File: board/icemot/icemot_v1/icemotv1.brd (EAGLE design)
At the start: 160 x 100 mm, 2 parts, among them U1 ICE40HX4K, U2 EFM32WG332FXXX-QFP64

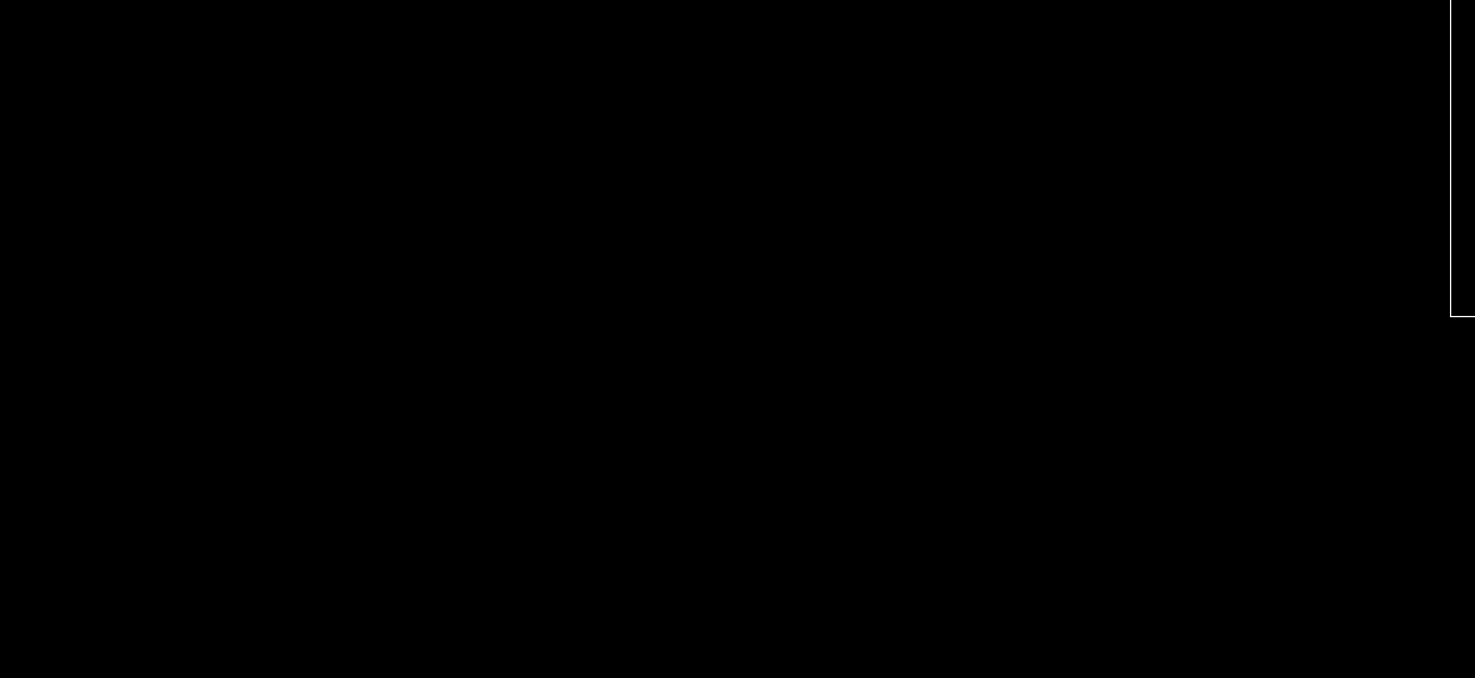
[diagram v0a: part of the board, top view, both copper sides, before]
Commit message: adding decoupling and usb connector
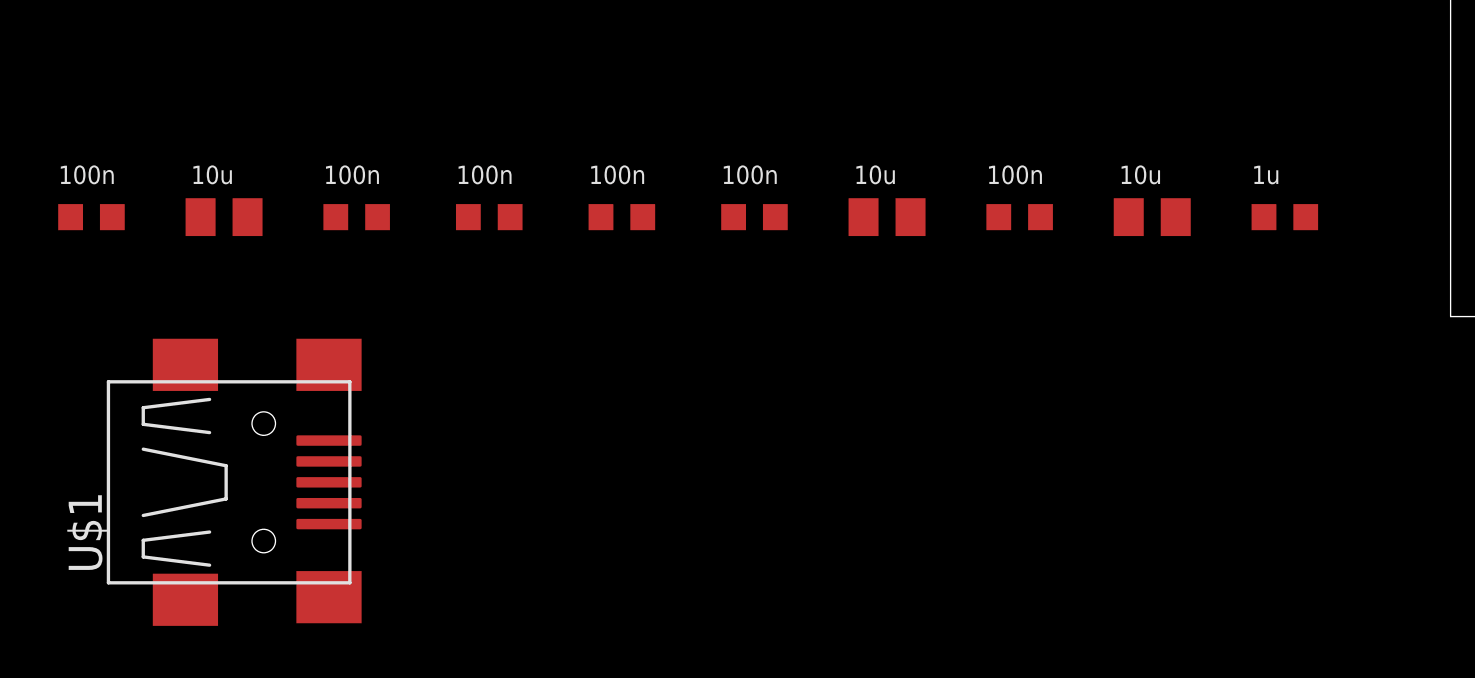
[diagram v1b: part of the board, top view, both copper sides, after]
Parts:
- added C1: 1u, standard_passive:R0603
- added C10, C3, C5, C6, C7, C8: 100n, standard_passive:R0603
- added C2, C4, C9: 10u, standard_passive:R0805
- added U$1: USB-SHIELD, usb-header:USB-M-S1
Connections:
- removed net DECOUPLE: U2.40
- removed net USBVREGI: U2.45
- removed net VDDREG: U2.39
- new net N$1: C1.1, U2.40
- new net N$2: U$1.D+, U2.48
- new net N$3: U$1.D-, U2.47
- new net N$4: U$1.VBUS, U2.45
- net +3V3: now also C10.2, C2.1, C3.1, C4.1, C5.1, C6.1, C7.1, C8.1, C9.1, U2.39
- net GND: now also C1.2, C10.1, C2.2, C3.2, C4.2, C5.2, C6.2, C7.2, C8.2, C9.2
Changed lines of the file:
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@@
 <element name="U1" library="ICE40HX" package="TQFP144" value="ICE40HX4K" x="45.72" y="48.26"/>
 <element name="U2" library="EFM32" package="TQFP64-0.5-12X12MM" value="EFM32WG332FXXX-QFP64" x="44.45" y="24.13"/>
+<element name="C1" library="standard_passive" package="R0603" value="1u" x="-6.35" y="3.81"/>
+<element name="C2" library="standard_passive" package="R0805" value="10u" x="-11.43" y="3.81"/>
+<element name="C3" library="standard_passive" package="R0603" value="100n" x="-16.51" y="3.81"/>
+<element name="C4" library="standard_passive" package="R0805" value="10u" x="-21.59" y="3.81"/>
+<element name="C5" library="standard_passive" package="R0603" value="100n" x="-26.67" y="3.81"/>
+<element name="C6" library="standard_passive" package="R0603" value="100n" x="-31.75" y="3.81"/>
+<element name="C7" library="standard_passive" package="R0603" value="100n" x="-36.83" y="3.81"/>
+<element name="C8" library="standard_passive" package="R0603" value="100n" x="-41.91" y="3.81"/>
+<element name="C9" library="standard_passive" package="R0805" value="10u" x="-46.99" y="3.81"/>
+<element name="C10" library="standard_passive" package="R0603" value="100n" x="-52.07" y="3.81"/>
+<element name="U$1" library="usb-header" package="USB-M-S1" value="USB-SHIELD" x="-45.72" y="-6.35"/>
 </elements>
 <signals>
@@
 <contactref element="U2" pad="56"/>
 <contactref element="U2" pad="8"/>
+<contactref element="C1" pad="2"/>
+<contactref element="C2" pad="2"/>
+<contactref element="C3" pad="2"/>
+<contactref element="C4" pad="2"/>
+<contactref element="C5" pad="2"/>
+<contactref element="C6" pad="2"/>
+<contactref element="C7" pad="2"/>
+<contactref element="C8" pad="2"/>
+<contactref element="C10" pad="1"/>
+<contactref element="C9" pad="2"/>
 <wire x1="56.32" y1="50.51" x2="56.32" y2="55.51" width="0" layer="19" extent="1-1"/>
 <wire x1="47.97" y1="58.86" x2="56.32" y2="55.51" width="0" layer="19" extent="1-1"/>
@@
 <wire x1="38.55" y1="24.38" x2="44.7" y2="30.03" width="0" layer="19" extent="1-1"/>
 <wire x1="43.2" y1="18.23" x2="38.55" y2="24.38" width="0" layer="19" extent="1-1"/>
+<wire x1="-5.55" y1="3.81" x2="38.55" y2="24.38" width="0" layer="19" extent="1-1"/>
+<wire x1="-10.53" y1="3.81" x2="-5.55" y2="3.81" width="0" layer="19" extent="1-1"/>
+<wire x1="-15.71" y1="3.81" x2="-10.53" y2="3.81" width="0" layer="19" extent="1-1"/>
+<wire x1="-20.69" y1="3.81" x2="-15.71" y2="3.81" width="0" layer="19" extent="1-1"/>
+<wire x1="-25.87" y1="3.81" x2="-20.69" y2="3.81" width="0" layer="19" extent="1-1"/>
+<wire x1="-30.95" y1="3.81" x2="-25.87" y2="3.81" width="0" layer="19" extent="1-1"/>
+<wire x1="-36.03" y1="3.81" x2="-30.95" y2="3.81" width="0" layer="19" extent="1-1"/>
+<wire x1="-41.11" y1="3.81" x2="-36.03" y2="3.81" width="0" layer="19" extent="1-1"/>
+<wire x1="-46.09" y1="3.81" x2="-41.11" y2="3.81" width="0" layer="19" extent="1-1"/>
+<wire x1="-52.87" y1="3.81" x2="-46.09" y2="3.81" width="0" layer="19" extent="1-1"/>
 </signal>
 <signal name="PLLGND">
@@
 <contactref element="U1" pad="109"/>
 </signal>
-<signal name="VDDREG">
-<contactref element="U2" pad="39"/>
-</signal>
-<signal name="DECOUPLE">
-<contactref element="U2" pad="40"/>
-</signal>
-<signal name="USBVREGI">
-<contactref element="U2" pad="45"/>
-</signal>
 <signal name="USBVREGO">
 <contactref element="U2" pad="46"/>
@@
 <contactref element="U2" pad="26"/>
 <contactref element="U2" pad="27"/>
+<contactref element="U2" pad="39"/>
+<contactref element="C3" pad="1"/>
+<contactref element="C2" pad="1"/>
+<contactref element="C4" pad="1"/>
+<contactref element="C5" pad="1"/>
+<contactref element="C6" pad="1"/>
+<contactref element="C7" pad="1"/>
+<contactref element="C8" pad="1"/>
+<contactref element="C10" pad="2"/>
+<contactref element="C9" pad="1"/>
+<wire x1="50.35" y1="23.38" x2="45.2" y2="30.03" width="0" layer="19" extent="1-1"/>
+<wire x1="45.7" y1="18.23" x2="50.35" y2="23.38" width="0" layer="19" extent="1-1"/>
+<wire x1="45.2" y1="18.23" x2="45.7" y2="18.23" width="0" layer="19" extent="1-1"/>
+<wire x1="43.7" y1="18.23" x2="45.2" y2="18.23" width="0" layer="19" extent="1-1"/>
 <wire x1="38.55" y1="24.88" x2="45.2" y2="30.03" width="0" layer="19" extent="1-1"/>
-<wire x1="43.7" y1="18.23" x2="38.55" y2="24.88" width="0" layer="19" extent="1-1"/>
-<wire x1="45.2" y1="18.23" x2="43.7" y2="18.23" width="0" layer="19" extent="1-1"/>
-<wire x1="45.7" y1="18.23" x2="45.2" y2="18.23" width="0" layer="19" extent="1-1"/>
+<wire x1="-12.33" y1="3.81" x2="38.55" y2="24.88" width="0" layer="19" extent="1-1"/>
+<wire x1="-17.31" y1="3.81" x2="-12.33" y2="3.81" width="0" layer="19" extent="1-1"/>
+<wire x1="-22.49" y1="3.81" x2="-17.31" y2="3.81" width="0" layer="19" extent="1-1"/>
+<wire x1="-27.47" y1="3.81" x2="-22.49" y2="3.81" width="0" layer="19" extent="1-1"/>
+<wire x1="-32.55" y1="3.81" x2="-27.47" y2="3.81" width="0" layer="19" extent="1-1"/>
+<wire x1="-37.63" y1="3.81" x2="-32.55" y2="3.81" width="0" layer="19" extent="1-1"/>
+<wire x1="-42.71" y1="3.81" x2="-37.63" y2="3.81" width="0" layer="19" extent="1-1"/>
+<wire x1="-47.89" y1="3.81" x2="-42.71" y2="3.81" width="0" layer="19" extent="1-1"/>
+<wire x1="-51.27" y1="3.81" x2="-47.89" y2="3.81" width="0" layer="19" extent="1-1"/>
+</signal>
+<signal name="N$1">
+<contactref element="U2" pad="40"/>
+<contactref element="C1" pad="1"/>
+<wire x1="-7.15" y1="3.81" x2="50.35" y2="23.88" width="0" layer="19" extent="1-1"/>
+</signal>
+<signal name="N$2">
+<contactref element="U$1" pad="D+"/>
+<contactref element="U2" pad="48"/>
+<wire x1="-42.97" y1="-6.35" x2="50.35" y2="27.94" width="0" layer="19" extent="1-1"/>
+</signal>
+<signal name="N$3">
+<contactref element="U$1" pad="D-"/>
+<contactref element="U2" pad="47"/>
+<wire x1="-42.97" y1="-5.55" x2="50.35" y2="27.38" width="0" layer="19" extent="1-1"/>
+</signal>
+<signal name="N$4">
+<contactref element="U$1" pad="VBUS"/>
+<contactref element="U2" pad="45"/>
+<wire x1="-42.97" y1="-4.75" x2="50.35" y2="26.38" width="0" layer="19" extent="1-1"/>
 </signal>
 </signals>

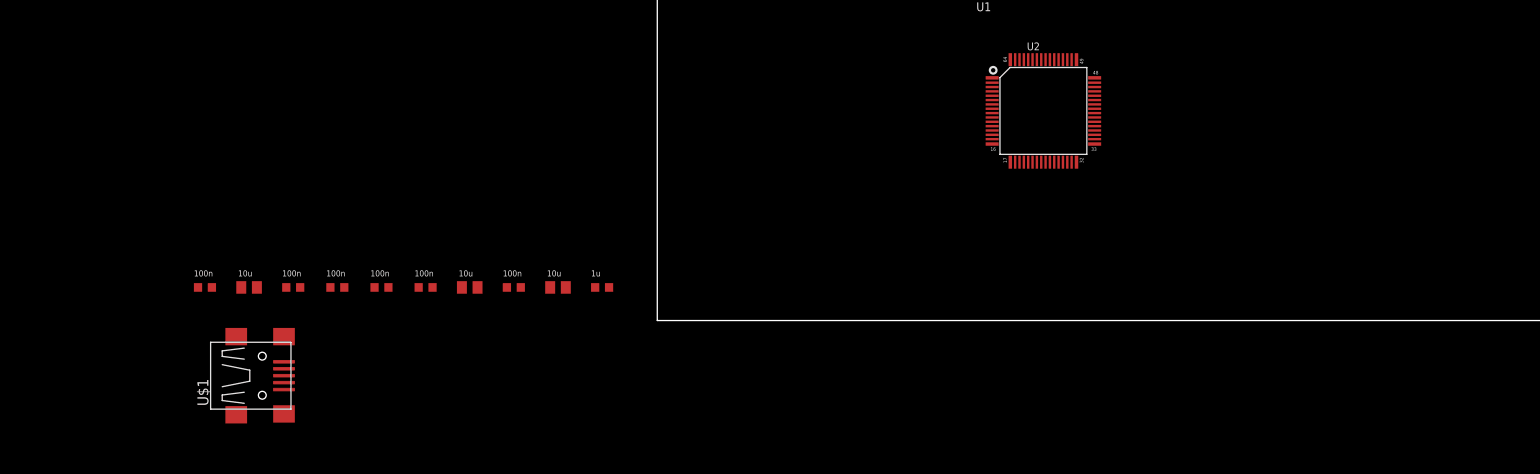
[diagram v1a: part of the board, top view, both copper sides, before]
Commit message: added xtal, usb to be checked
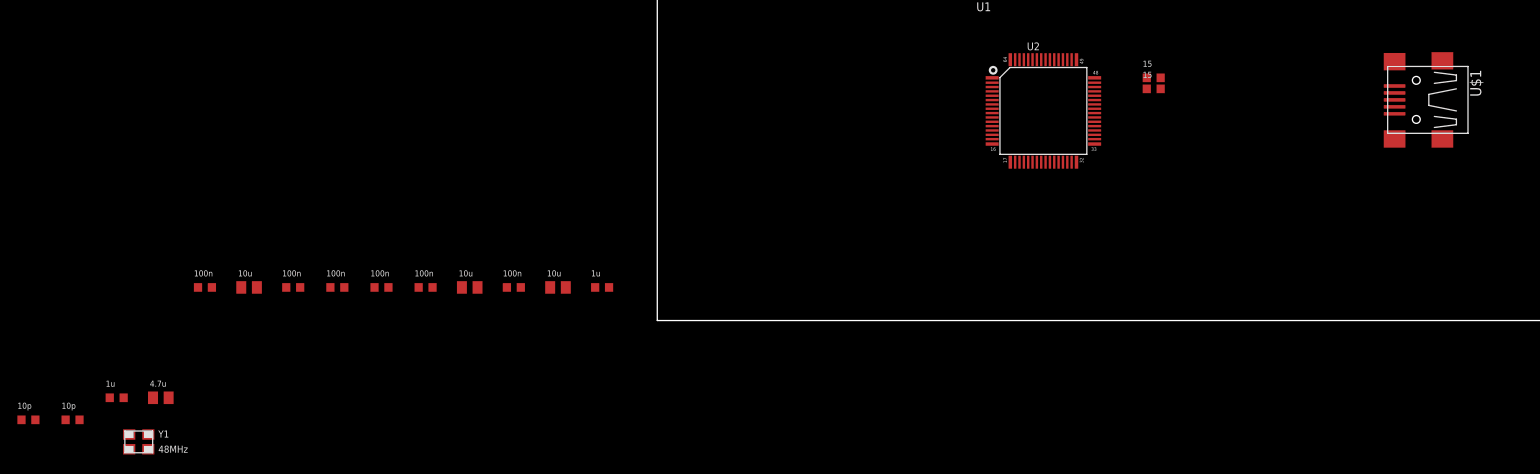
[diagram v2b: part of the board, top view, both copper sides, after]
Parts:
- added C11: 4.7u, standard_passive:R0805
- added C12: 1u, standard_passive:R0603
- added C13, C14: 10p, standard_passive:R0603
- added R1, R2: 15, standard_passive:R0603
- added Y1: 48MHz, xtals:3.2X2.5MM
- moved U$1 137.1 mm to (87.6, 25.4), turned to 180 degrees
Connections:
- removed net USBVREGO: U2.46
- new net N$5: C12.2, U2.46
- new net N$6: R2.2, U$1.D+
- new net N$7: R2.1, U2.48
- new net N$8: C13.1, U2.25, Y1.3
- new net N$9: C14.1, U2.24, Y1.1
- net GND: now also C11.2, C12.1, C13.2, C14.2, U$1.GND, U$1.GND@1, U$1.GND@2, U$1.GND@3, U$1.GND@4
- net N$2: now also R1.1, U2.47; no longer U$1.D+, U2.48
- net N$3: now also R1.2; no longer U2.47
- net N$4: now also C11.1, U2.52
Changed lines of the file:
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@@
 <element name="C9" library="standard_passive" package="R0805" value="10u" x="-46.99" y="3.81"/>
 <element name="C10" library="standard_passive" package="R0603" value="100n" x="-52.07" y="3.81"/>
-<element name="U$1" library="usb-header" package="USB-M-S1" value="USB-SHIELD" x="-45.72" y="-6.35"/>
+<element name="U$1" library="usb-header" package="USB-M-S1" value="USB-SHIELD" x="87.63" y="25.4" rot="R180"/>
+<element name="C11" library="standard_passive" package="R0805" value="4.7u" x="-57.15" y="-8.89"/>
+<element name="C12" library="standard_passive" package="R0603" value="1u" x="-62.23" y="-8.89"/>
+<element name="R1" library="standard_passive" package="R0603" value="15" x="57.15" y="26.67"/>
+<element name="R2" library="standard_passive" package="R0603" value="15" x="57.15" y="27.94"/>
+<element name="Y1" library="xtals" package="3.2X2.5MM" value="48MHz" x="-59.69" y="-13.97"/>
+<element name="C13" library="standard_passive" package="R0603" value="10p" x="-67.31" y="-11.43"/>
+<element name="C14" library="standard_passive" package="R0603" value="10p" x="-72.39" y="-11.43"/>
 </elements>
 <signals>
@@
 <contactref element="C10" pad="1"/>
 <contactref element="C9" pad="2"/>
-<wire x1="56.32" y1="50.51" x2="56.32" y2="55.51" width="0" layer="19" extent="1-1"/>
+<contactref element="U$1" pad="GND@1"/>
+<contactref element="U$1" pad="GND@2"/>
+<contactref element="U$1" pad="GND@3"/>
+<contactref element="U$1" pad="GND@4"/>
+<contactref element="U$1" pad="GND"/>
+<contactref element="C11" pad="2"/>
+<contactref element="C12" pad="1"/>
+<contactref element="C14" pad="2"/>
+<contactref element="C13" pad="2"/>
+<wire x1="84.88" y1="29.8" x2="90.38" y2="29.9" width="0" layer="19" extent="1-1"/>
+<wire x1="84.88" y1="27" x2="84.88" y2="29.8" width="0" layer="19" extent="1-1"/>
+<wire x1="84.88" y1="20.9" x2="84.88" y2="27" width="0" layer="19" extent="1-1"/>
+<wire x1="90.38" y1="20.9" x2="84.88" y2="20.9" width="0" layer="19" extent="1-1"/>
+<wire x1="56.32" y1="50.51" x2="84.88" y2="29.8" width="0" layer="19" extent="1-1"/>
+<wire x1="56.32" y1="55.51" x2="56.32" y2="50.51" width="0" layer="19" extent="1-1"/>
 <wire x1="47.97" y1="58.86" x2="56.32" y2="55.51" width="0" layer="19" extent="1-1"/>
 <wire x1="39.47" y1="58.86" x2="47.97" y2="58.86" width="0" layer="19" extent="1-1"/>
@@
 <wire x1="-46.09" y1="3.81" x2="-41.11" y2="3.81" width="0" layer="19" extent="1-1"/>
 <wire x1="-52.87" y1="3.81" x2="-46.09" y2="3.81" width="0" layer="19" extent="1-1"/>
+<wire x1="-56.25" y1="-8.89" x2="-52.87" y2="3.81" width="0" layer="19" extent="1-1"/>
+<wire x1="-63.03" y1="-8.89" x2="-56.25" y2="-8.89" width="0" layer="19" extent="1-1"/>
+<wire x1="-66.51" y1="-11.43" x2="-63.03" y2="-8.89" width="0" layer="19" extent="1-1"/>
+<wire x1="-71.59" y1="-11.43" x2="-66.51" y2="-11.43" width="0" layer="19" extent="1-1"/>
 </signal>
 <signal name="PLLGND">
@@
 <signal name="VPP_FAST">
 <contactref element="U1" pad="109"/>
-</signal>
-<signal name="USBVREGO">
-<contactref element="U2" pad="46"/>
 </signal>
 <signal name="+3V3">
@@
 <wire x1="-7.15" y1="3.81" x2="50.35" y2="23.88" width="0" layer="19" extent="1-1"/>
 </signal>
-<signal name="N$2">
-<contactref element="U$1" pad="D+"/>
-<contactref element="U2" pad="48"/>
-<wire x1="-42.97" y1="-6.35" x2="50.35" y2="27.94" width="0" layer="19" extent="1-1"/>
-</signal>
-<signal name="N$3">
-<contactref element="U$1" pad="D-"/>
-<contactref element="U2" pad="47"/>
-<wire x1="-42.97" y1="-5.55" x2="50.35" y2="27.38" width="0" layer="19" extent="1-1"/>
-</signal>
 <signal name="N$4">
 <contactref element="U$1" pad="VBUS"/>
 <contactref element="U2" pad="45"/>
-<wire x1="-42.97" y1="-4.75" x2="50.35" y2="26.38" width="0" layer="19" extent="1-1"/>
+<contactref element="C11" pad="1"/>
+<contactref element="U2" pad="52"/>
+<wire x1="50.35" y1="26.38" x2="84.88" y2="23.8" width="0" layer="19" extent="1-1"/>
+<wire x1="46.7" y1="30.03" x2="50.35" y2="26.38" width="0" layer="19" extent="1-1"/>
+<wire x1="-58.05" y1="-8.89" x2="46.7" y2="30.03" width="0" layer="19" extent="1-1"/>
+</signal>
+<signal name="N$5">
+<contactref element="U2" pad="46"/>
+<contactref element="C12" pad="2"/>
+<wire x1="-61.43" y1="-8.89" x2="50.35" y2="26.88" width="0" layer="19" extent="1-1"/>
+</signal>
+<signal name="N$2">
+<contactref element="U2" pad="47"/>
+<contactref element="R1" pad="1"/>
+<wire x1="56.35" y1="26.67" x2="50.35" y2="27.38" width="0" layer="19" extent="1-1"/>
+</signal>
+<signal name="N$3">
+<contactref element="R1" pad="2"/>
+<contactref element="U$1" pad="D-"/>
+<wire x1="84.88" y1="24.6" x2="57.95" y2="26.67" width="0" layer="19" extent="1-1"/>
+</signal>
+<signal name="N$6">
+<contactref element="U$1" pad="D+"/>
+<contactref element="R2" pad="2"/>
+<wire x1="84.88" y1="25.4" x2="57.95" y2="27.94" width="0" layer="19" extent="1-1"/>
+</signal>
+<signal name="N$7">
+<contactref element="R2" pad="1"/>
+<contactref element="U2" pad="48"/>
+<wire x1="50.35" y1="27.94" x2="56.35" y2="27.94" width="0" layer="19" extent="1-1"/>
+</signal>
+<signal name="N$8">
+<contactref element="Y1" pad="3"/>
+<contactref element="U2" pad="25"/>
+<contactref element="C13" pad="1"/>
+<wire x1="-58.59" y1="-13.12" x2="-68.11" y2="-11.43" width="0" layer="19" extent="1-1"/>
+<wire x1="44.7" y1="18.23" x2="-58.59" y2="-13.12" width="0" layer="19" extent="1-1"/>
+</signal>
+<signal name="N$9">
+<contactref element="Y1" pad="1"/>
+<contactref element="U2" pad="24"/>
+<contactref element="C14" pad="1"/>
+<wire x1="-60.79" y1="-14.82" x2="-73.19" y2="-11.43" width="0" layer="19" extent="1-1"/>
+<wire x1="44.2" y1="18.23" x2="-60.79" y2="-14.82" width="0" layer="19" extent="1-1"/>
 </signal>
 </signals>

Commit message: starting ICE schematic
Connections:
- net VCC renamed +1V2
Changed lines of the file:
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@@
 <wire x1="35.12" y1="48.51" x2="56.32" y2="48.01" width="0" layer="19" extent="1-1"/>
-</signal>
-<signal name="VCC">
-<contactref element="U1" pad="27"/>
-<contactref element="U1" pad="40"/>
-<contactref element="U1" pad="92"/>
-<contactref element="U1" pad="111"/>
-<wire x1="35.12" y1="56.01" x2="44.97" y2="58.86" width="0" layer="19" extent="1-1"/>
-<wire x1="56.32" y1="41.01" x2="44.97" y2="58.86" width="0" layer="19" extent="1-1"/>
-<wire x1="49.97" y1="37.66" x2="56.32" y2="41.01" width="0" layer="19" extent="1-1"/>
 </signal>
 <signal name="VPP_2V5">
@@
 <wire x1="44.2" y1="18.23" x2="-60.79" y2="-14.82" width="0" layer="19" extent="1-1"/>
 </signal>
+<signal name="+1V2">
+<contactref element="U1" pad="111"/>
+<contactref element="U1" pad="92"/>
+<contactref element="U1" pad="40"/>
+<contactref element="U1" pad="27"/>
+<wire x1="35.12" y1="56.01" x2="44.97" y2="58.86" width="0" layer="19" extent="1-1"/>
+<wire x1="56.32" y1="41.01" x2="44.97" y2="58.86" width="0" layer="19" extent="1-1"/>
+<wire x1="49.97" y1="37.66" x2="56.32" y2="41.01" width="0" layer="19" extent="1-1"/>
+</signal>
 </signals>
